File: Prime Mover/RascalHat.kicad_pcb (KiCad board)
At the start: 2 copper layers, 75 x 56 mm, 53 parts, among them J1 Conn_01x08_Male, J10 Conn_01x04_Male, J11 Conn_01x03_Male, J12 Conn_01x03_Male, J13 Conn_01x07_Male, J14 Conn_01x07_Male, J15 Conn_01x07_Male, J16 Conn_01x06_Male, J17 Conn_01x02_Male, J18 Conn_01x07_Male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

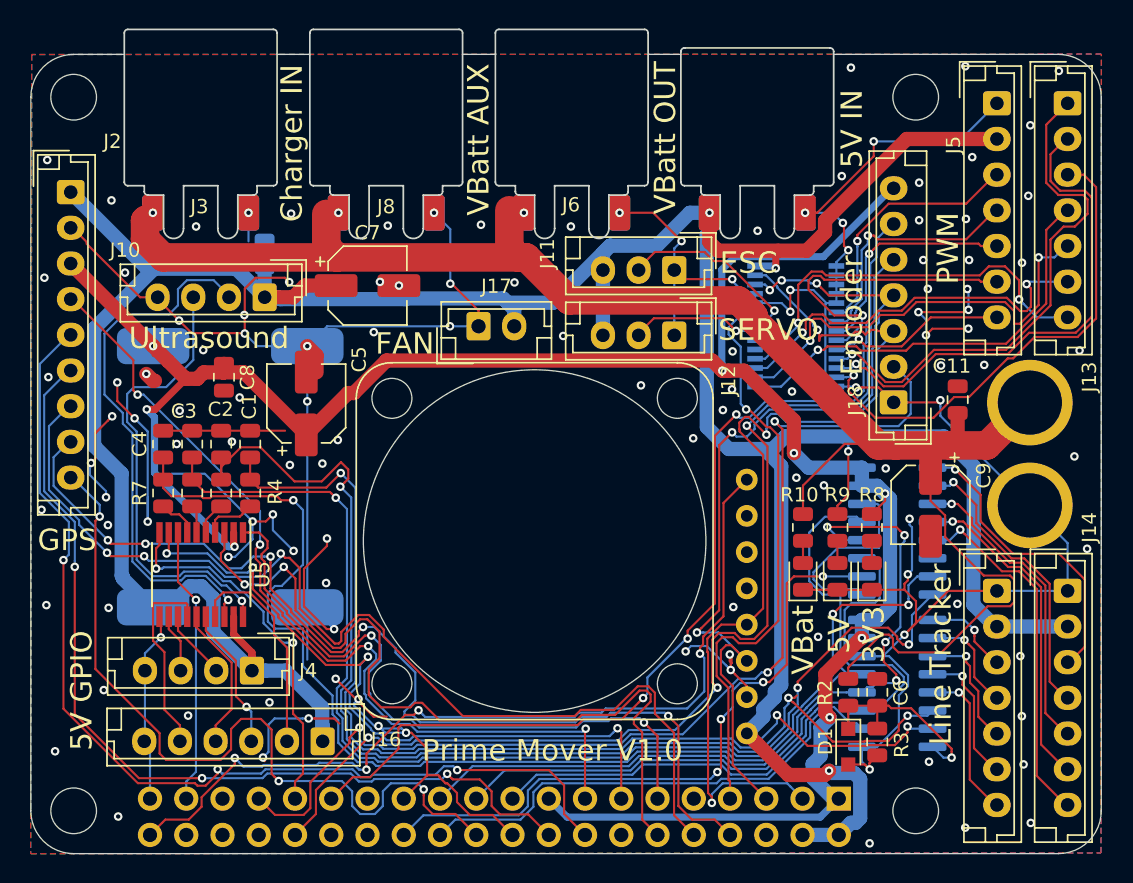
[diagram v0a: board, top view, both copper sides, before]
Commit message: pcb XT60 location adjusted, i2C pullup resistors added
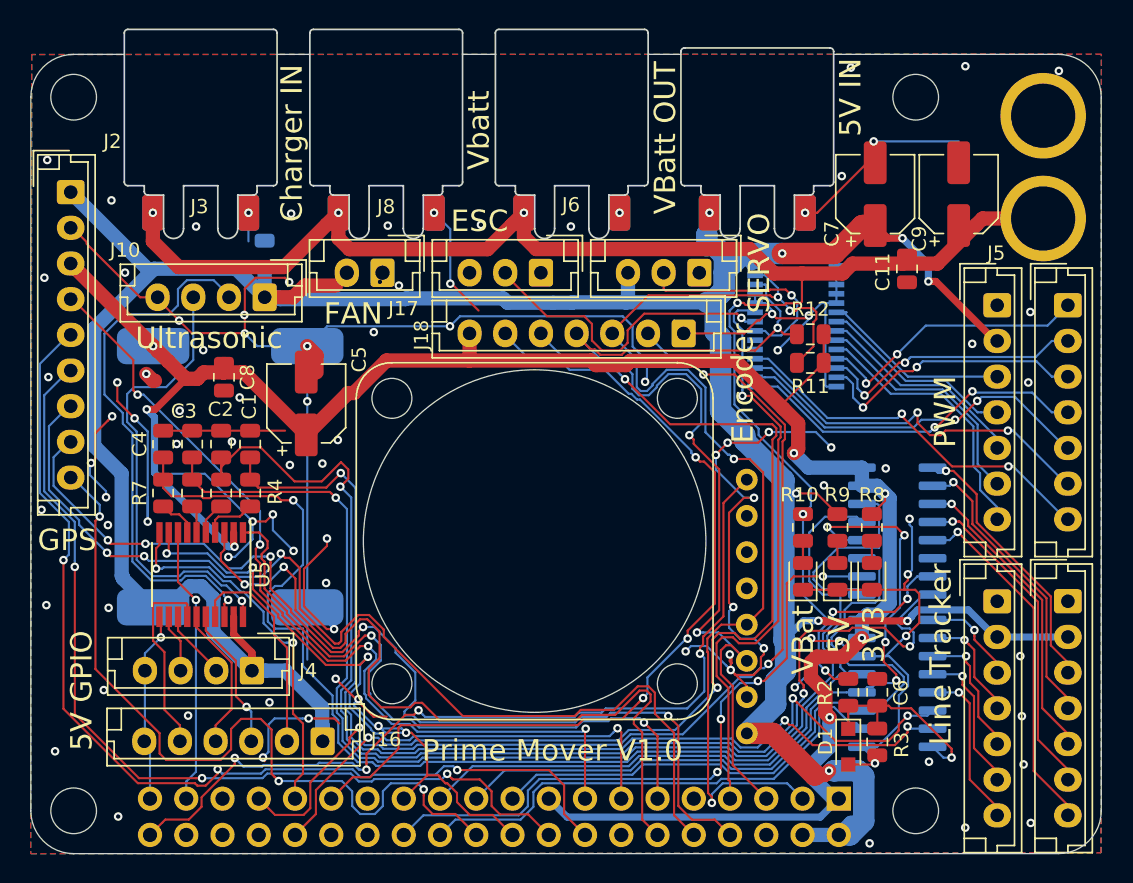
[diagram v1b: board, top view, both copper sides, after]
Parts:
- added R11: 4k7, Resistor_SMD:R_0805_2012Metric, F.Cu at (54.6, 21.6)
- added R12: 4k7, Resistor_SMD:R_0805_2012Metric, F.Cu at (54.6, 19.6)
- moved C7 36.1 mm to (59.2, 9.79), turned to 90 degrees
- moved C9 21.9 mm to (65.0, 9.79), turned to 90 degrees
- moved J9 20.1 mm to (70.9, 7.90), turned to 270 degrees
- moved J18 15.5 mm to (45.7, 19.6), turned to 180 degrees
- moved J13 14.2 mm to (72.7, 17.6)
- moved J5 14.2 mm to (67.7, 17.6)
- moved C11 9.82 mm to (61.4, 15.0), turned to 270 degrees
- moved J11 9.35 mm to (35.7, 15.3)
- moved J17 7.70 mm to (24.6, 15.3), turned to 180 degrees
- moved J12 4.72 mm to (46.8, 15.3)
- moved J15 0.73 mm to (67.7, 38.3)
- moved J14 0.73 mm to (72.7, 38.3)
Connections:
- J11 pad 3: +5V -> Net-(J11-Pad3)
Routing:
- net /PWM_PCA9685/P5: track 36.7 -> 19.4 mm, vias 1 -> 2
- net /PWM_PCA9685/P6: track 35.9 -> 19.0 mm, vias 1 -> 2
- net /PWM_PCA9685/P7: track 35.1 -> 19.4 mm, vias 1 -> 2
- net GND: track 342.6 -> 331.3 mm, vias 125 -> 101
- net +3V3: track 159.2 -> 148.2 mm, vias 8 -> 7
- net +5V: track 243.3 -> 232.5 mm, vias 4 -> 8
- net PWM_ESC: track 13.6 -> 22.3 mm
- net ENC_OUT: track 70.7 -> 62.5 mm
- net I2C_SCL: track 63.0 -> 71.0 mm, vias 5 -> 3
- net +BATT: track 121.8 -> 114.4 mm, vias 3 -> 6
- net I2C_SDA: track 68.2 -> 75.5 mm, vias 3 -> 4
- net PWM_Servo: track 9.10 -> 15.7 mm
- net /PWM_PCA9685/P4: track 12.6 -> 19.0 mm, vias 1 -> 0
- net /PWM_PCA9685/P8: track 30.3 -> 25.0 mm, vias 1 -> 2
- net /PWM_PCA9685/P9: track 30.7 -> 25.7 mm
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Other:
- board text added: "Ultrasonic"
- board text added: "Vbatt"
- board text removed: "Ultrasound"
- board text removed: "VBatt AUX"
